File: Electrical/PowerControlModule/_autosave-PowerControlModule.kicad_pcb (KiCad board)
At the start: 4 copper layers, 47 parts, among them J1 178.6164.0002, J10 Screw_Terminal_01x02, J11 Screw_Terminal_01x02, J12 Screw_Terminal_01x02, J13 Screw_Terminal_01x02, J14 Screw_Terminal_01x02, J15 Screw_Terminal_01x02, J16 Screw_Terminal_01x02, J17 Conn_01x03, J2 178.6164.0002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

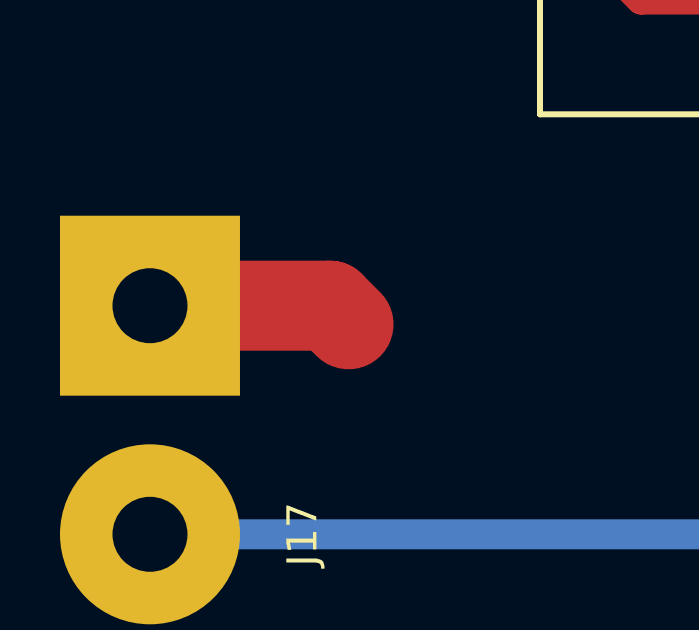
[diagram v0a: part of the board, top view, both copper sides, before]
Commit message: Routes PCM as a 4 layer board
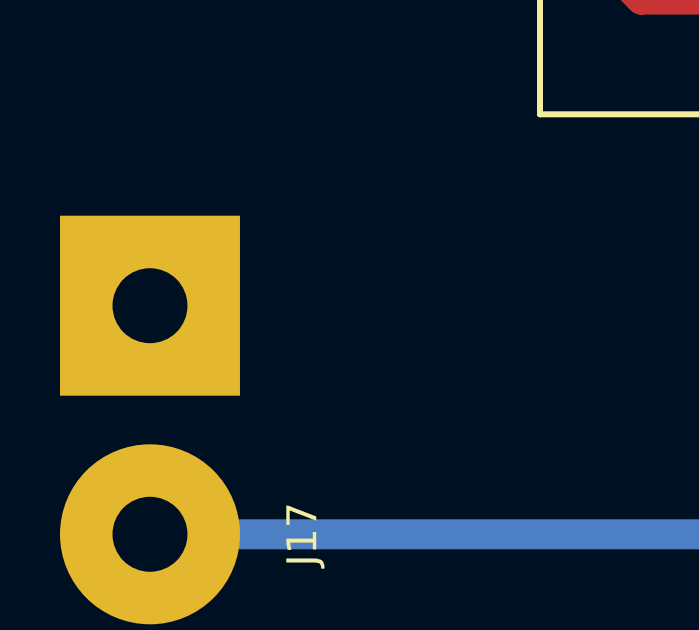
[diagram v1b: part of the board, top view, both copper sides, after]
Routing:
- net +12V: track 6.88 -> 0.00 mm
- added copper zone on In1.Cu, net +12V
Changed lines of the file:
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@@
     (thickness 1.6)
     (drawings 0)
-    (tracks 113)
+    (tracks 111)
     (zones 0)
     (modules 47)
@@
     (via_min_size 0.4)
     (via_min_drill 0.3)
+    (blind_buried_vias_allowed yes)
     (uvia_size 0.3)
     (uvia_drill 0.1)
@@
   (segment (start 432.8 -18.28) (end 430.08 -21) (width 1) (layer F.Cu) (net 14))
   (segment (start 432.8 -5.6) (end 432.8 -18.28) (width 1) (layer F.Cu) (net 14))
-  (segment (start 307.99974 15.38) (end 308.61974 16) (width 3) (layer F.Cu) (net 15))
-  (segment (start 302 15.38) (end 307.99974 15.38) (width 3) (layer F.Cu) (net 15))
   (segment (start 374.610001 36.929999) (end 375.54 36) (width 1) (layer F.Cu) (net 16))
   (segment (start 373.909999 37.630001) (end 374.610001 36.929999) (width 1) (layer F.Cu) (net 16))
@@
   (segment (start 341 23) (end 302 23) (width 1) (layer B.Cu) (net 43))
   (segment (start 345 19) (end 341 23) (width 1) (layer B.Cu) (net 43))
+  (zone (net 15) (net_name +12V) (layer In1.Cu) (hatch edge 0.508)
+    (connect_pads (clearance 0.508))
+    (min_thickness 0.254)
+    (fill yes (arc_segments 32) (thermal_gap 0.508) (thermal_bridge_width 0.508))
+    (polygon
+      (pts
+        (xy 293 -28) (xy 292 252) (xy 442 252) (xy 442 -28)
+      )
+    )
+  )
 )
